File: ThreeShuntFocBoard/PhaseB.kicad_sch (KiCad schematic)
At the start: 40 parts, among them J10 Conn_01x01, Q1 MMBT5551L, Q10 IRF540N, Q2 SS8050, Q3 SS8550, Q4 SS8550, Q5 SS8550, Q6 SS8550, Q7 IRF540N, Q8 IRF540N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

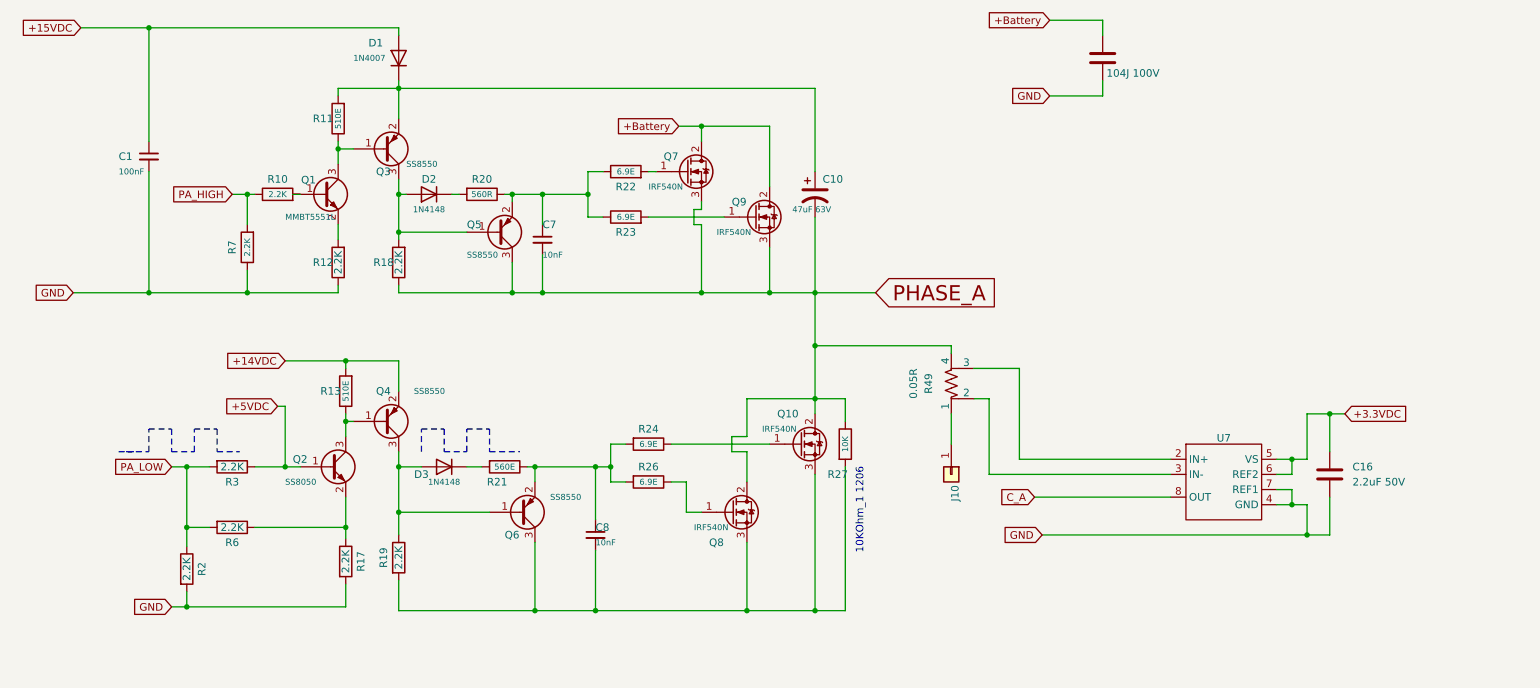
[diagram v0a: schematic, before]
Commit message: commit 2:  Updated Power Supply, Safety Fuse, Phase Design, and Hall Sensor Circuit
for more details read ChangesDetial.txt in same folder.
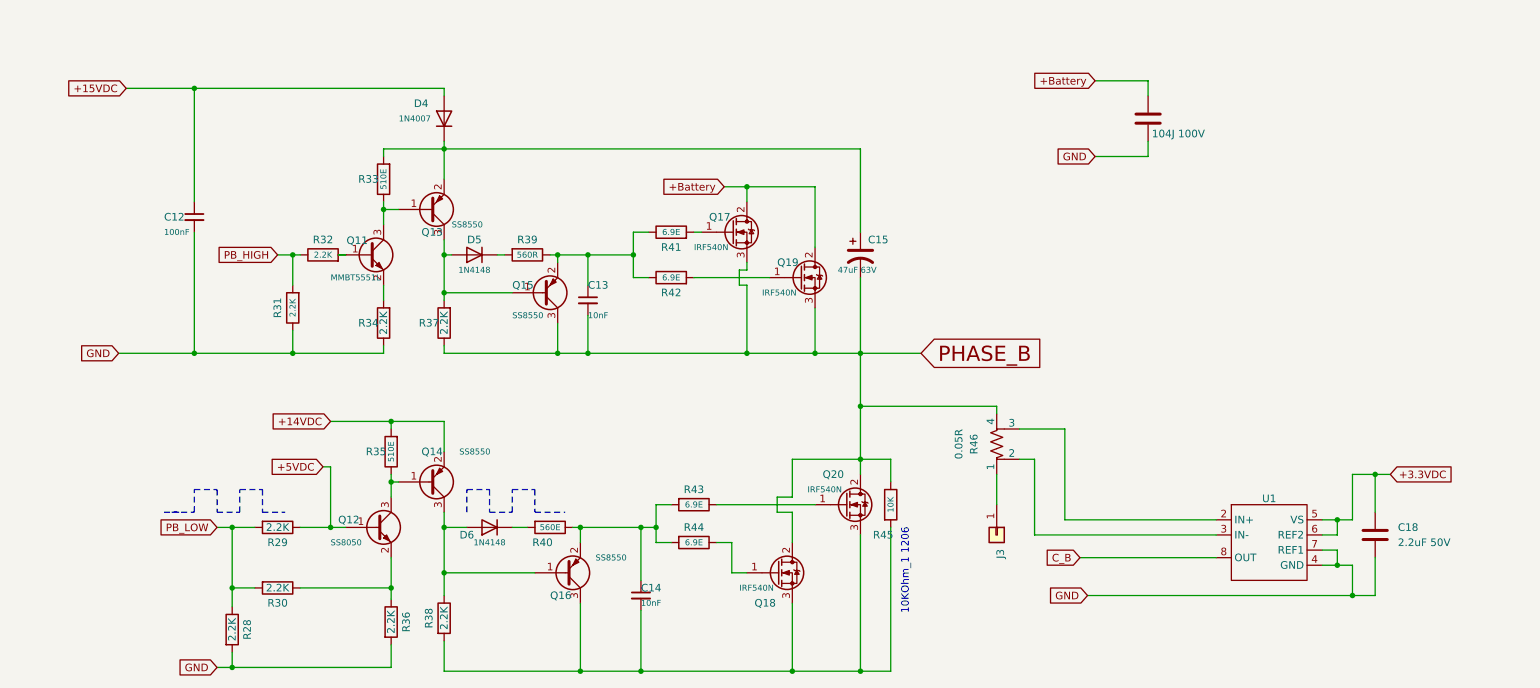
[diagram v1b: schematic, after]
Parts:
- removed C1: 100nF, Footprints:C_0603, symbol Device:C_Small
- removed C10: 47uF 63V, BLDC:220uF63V, symbol Device:C_Polarized_US
- removed C11: 104J 100V, Footprints:104J_100V, symbol Device:C
- removed C16: 2.2uF 50V, symbol Device:C
- removed C7, C8: 10nF, Footprints:C_0603, symbol Device:C_Small
- removed D1: 1N4007, BLDC:ZenerDiode_S1M, symbol Diode:1N4007
- removed D2, D3: 1N4148, Footprints:SOD_123_v1, symbol Diode:1N4148
- removed J10: Conn_01x01, Footprints:Powe_pad, symbol Connector_Generic:Conn_01x01
- removed Q1: MMBT5551L, Footprints:SOT-23_v1, symbol Transistor_BJT:MMBT5551L
- removed Q10, Q7, Q8, Q9: IRF540N, BLDC:TO-220-3_Vertical, symbol Transistor_FET:IRF540N
- removed Q2: SS8050, Footprints:SOT-23_v1, symbol Transistor_BJT:S8050
- removed Q3, Q4, Q5, Q6: SS8550, Footprints:SOT-23_v1, symbol Transistor_BJT:S8550
- removed R10, R12, R17, R18, R19, R2, R3, R6, R7: 2.2K, Footprints:R_0603, symbol Device:R
- removed R11, R13: 510E, Footprints:R_0603, symbol Device:R
- removed R20: 560R, Footprints:R_0603, symbol Device:R
- removed R21: 560E, Footprints:R_0603, symbol Device:R
- removed R22, R23, R24, R26: 6.9E, Footprints:R_0603, symbol Device:R
- removed R27: 10K, Footprints:1206_R, symbol Device:R
- removed R49: 0.05R, symbol Device:R_Shunt_US
- removed U7: ~, symbol Symbol_lib:INA240
- added C12: 100nF, Footprints:C_0603, symbol Device:C_Small
- added C13, C14: 10nF, Footprints:C_0603, symbol Device:C_Small
- added C15: 47uF 63V, BLDC:220uF63V, symbol Device:C_Polarized_US
- added C17: 104J 100V, Footprints:104J_100V, symbol Device:C
- added C18: 2.2uF 50V, symbol Device:C
- added D4: 1N4007, BLDC:ZenerDiode_S1M, symbol Diode:1N4007
- added D5, D6: 1N4148, Footprints:SOD_123_v1, symbol Diode:1N4148
- added J3: Conn_01x01, Footprints:Powe_pad, symbol Connector_Generic:Conn_01x01
- added Q11: MMBT5551L, Footprints:SOT-23_v1, symbol Transistor_BJT:MMBT5551L
- added Q12: SS8050, Footprints:SOT-23_v1, symbol Transistor_BJT:S8050
- added Q13, Q14, Q15, Q16: SS8550, Footprints:SOT-23_v1, symbol Transistor_BJT:S8550
- added Q17, Q18, Q19, Q20: IRF540N, BLDC:TO-220-3_Vertical, symbol Transistor_FET:IRF540N
- added R28, R29, R30, R31, R32, R34, R36, R37, R38: 2.2K, Footprints:R_0603, symbol Device:R
- added R33, R35: 510E, Footprints:R_0603, symbol Device:R
- added R39: 560R, Footprints:R_0603, symbol Device:R
- added R40: 560E, Footprints:R_0603, symbol Device:R
- added R41, R42, R43, R44: 6.9E, Footprints:R_0603, symbol Device:R
- added R45: 10K, Footprints:1206_R, symbol Device:R
- added R46: 0.05R, symbol Device:R_Shunt_US
- added U1: ~, symbol Symbol_lib:INA240
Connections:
- net +14VDC: now also Q14.2 (E), R35.2
- net +15VDC: now also C12.1, D4.2 (A)
- net +3.3VDC: now also C18.1, U1.5 (VS), U1.6 (REF2)
- net +5VDC: now also Q12.1 (B), R29.1
- net +Battery: now also C17.1, Q17.2 (D), Q19.2 (D)
- net GND: now also C12.2, C17.2, C18.2, R28.2, R31.1, R34.1, R36.2, U1.4 (GND), U1.7 (REF1)
- new net: Q11.2 (E), R34.2
- new net: Q11.1 (B), R32.2
- new net: Q20.1 (G), R43.1
- new net: C14.2, Q16.3 (C), Q18.3 (S), Q20.3 (S), R38.2, R45.2
- new net: Q11.3 (C), Q13.1 (B), R33.1
- new net: C15.1, D4.1 (K), Q13.2 (E), R33.2
- new net: Q12.3 (C), Q14.1 (B), R35.1
- new net: Q19.1 (G), R42.2
- new net: D6.2 (A), Q14.3 (C), Q16.1 (B), R38.1
- new net: Q18.1 (G), R44.1
- new net: C14.1, Q16.2 (E), R40.1, R43.2, R44.2
- new net: R46.3, U1.2 (IN+)
- new net: R46.2, U1.3 (IN-)
- new net: J3.1 (Pin_1), R46.1
- new net: Q17.1 (G), R41.2
- new net: C13.1, Q15.2 (E), R39.1, R41.1, R42.1
- new net: D5.1 (K), R39.2
- new net: D5.2 (A), Q13.3 (C), Q15.1 (B), R37.2
- new net: Q12.2 (E), R30.1, R36.1
- new net: D6.1 (K), R40.2
- new net C_B: U1.8 (OUT)
- new net PB_HIGH: R31.2, R32.1
- new net PB_LOW: R28.1, R29.2, R30.2
- new net PHASE_B: C13.2, C15.2, Q15.3 (C), Q17.3 (S), Q18.2 (D), Q19.3 (S), Q20.2 (D), R37.1, R45.1, R46.4

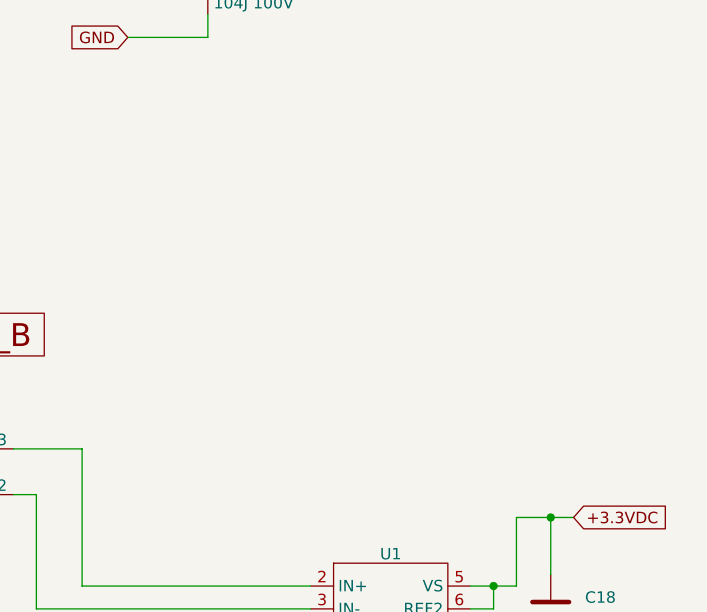
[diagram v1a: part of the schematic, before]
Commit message: Commit 3: Assigned STM32G431C6Tx (LQFP-48) pins as per the shared Excel, peripheral connections WIP, Phase C current sensing removed due to ADC group limitations
read attach excel files and changesDetails.txt file for more detail
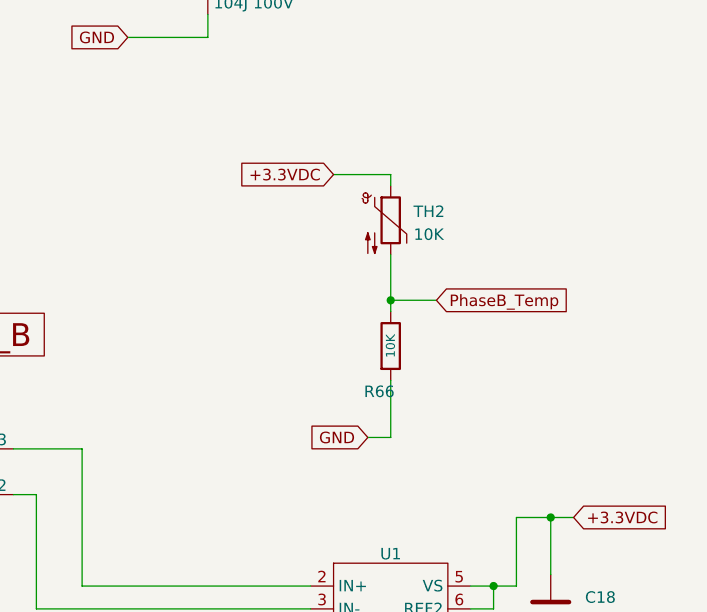
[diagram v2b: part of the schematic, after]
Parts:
- added R66: 10K, Footprints:1206_R, symbol Device:R
- added TH2: 10K, symbol Device:Thermistor_NTC
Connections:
- net +3.3VDC: now also TH2.1
- net GND: now also R66.2
- new net PhaseB_Temp: R66.1, TH2.2

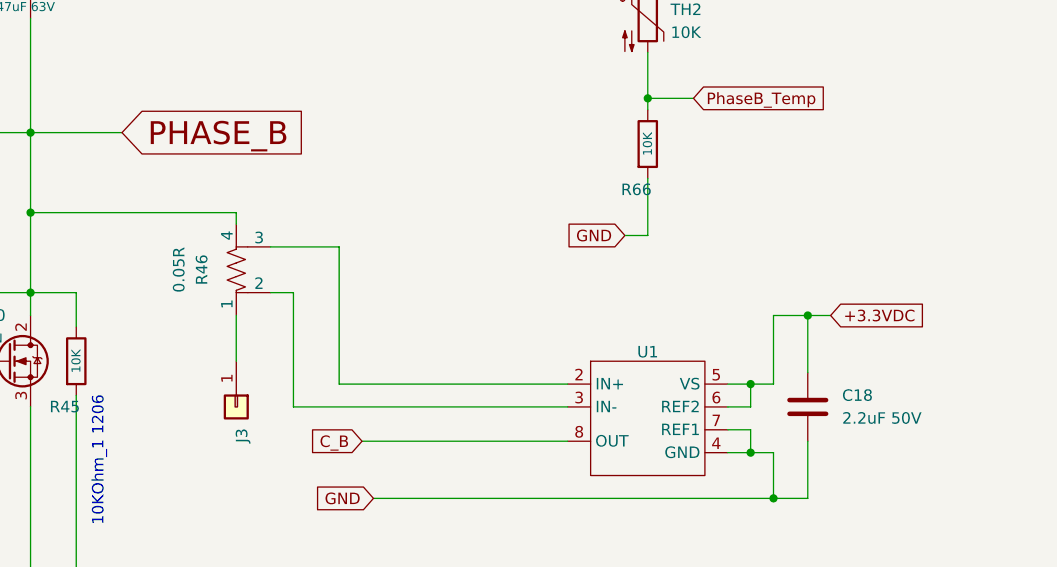
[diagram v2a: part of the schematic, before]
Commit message: Commit 5: Improved power integrity and ADC accuracy.
for more details read changesDetail.txt file
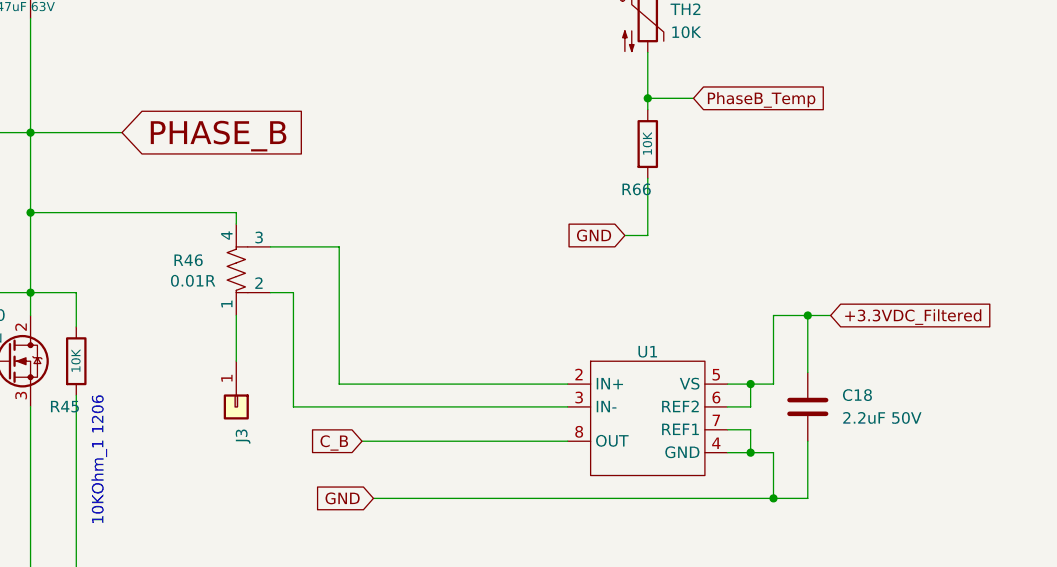
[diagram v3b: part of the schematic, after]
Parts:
- R46: value 0.05R -> 0.01R
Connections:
- net +3.3VDC: no longer C18.1, U1.5 (VS), U1.6 (REF2)
- new net +3.3VDC_Filtered: C18.1, U1.5 (VS), U1.6 (REF2)
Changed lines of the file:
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@@
+		)
+	)
+	(global_label "+3.3VDC_Filtered"
+		(shape input)
+		(at 256.54 96.52 0)
+		(fields_autoplaced yes)
+		(effects
+			(font
+				(size 1.27 1.27)
+			)
+			(justify left)
+		)
+		(property "Intersheetrefs" "${INTERSHEET_REFS}"
+			(at 275.9143 96.52 0)
+			(effects
+				(font
+					(size 1.27 1.27)
+				)
+				(justify left)
+				(hide yes)
+			)
 		)
 	)
@@
 		)
 	)
-	(global_label "+3.3VDC"
-		(shape input)
-		(at 256.54 96.52 0)
-		(fields_autoplaced yes)
-		(effects
-			(font
-				(size 1.27 1.27)
-			)
-			(justify left)
-		)
-		(property "Intersheetrefs" "${INTERSHEET_REFS}"
-			(at 267.75 96.52 0)
-			(effects
-				(font
-					(size 1.27 1.27)
-				)
-				(justify left)
-				(hide yes)
-			)
-		)
-	)
 	(global_label "GND"
 		(shape input)
@@
 		(dnp no)
 		(property "Reference" "R46"
-			(at 186.69 91.44 90)
-			(effects
-				(font
-					(size 1.27 1.27)
-				)
-			)
-		)
-		(property "Value" "0.05R"
-			(at 184.15 91.44 90)
-			(effects
-				(font
+			(at 185.166 90.424 0)
+			(effects
+				(font
+					(size 1.27 1.27)
+				)
+			)
+		)
+		(property "Value" "0.01R"
+			(at 185.674 92.71 0)
+			(effects
+				(font
